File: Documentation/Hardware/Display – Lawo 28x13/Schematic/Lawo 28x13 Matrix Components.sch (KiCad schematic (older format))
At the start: 7 parts, among them IC1 FP2800A, P1 CONN_02X17, P2 CONN_01X03

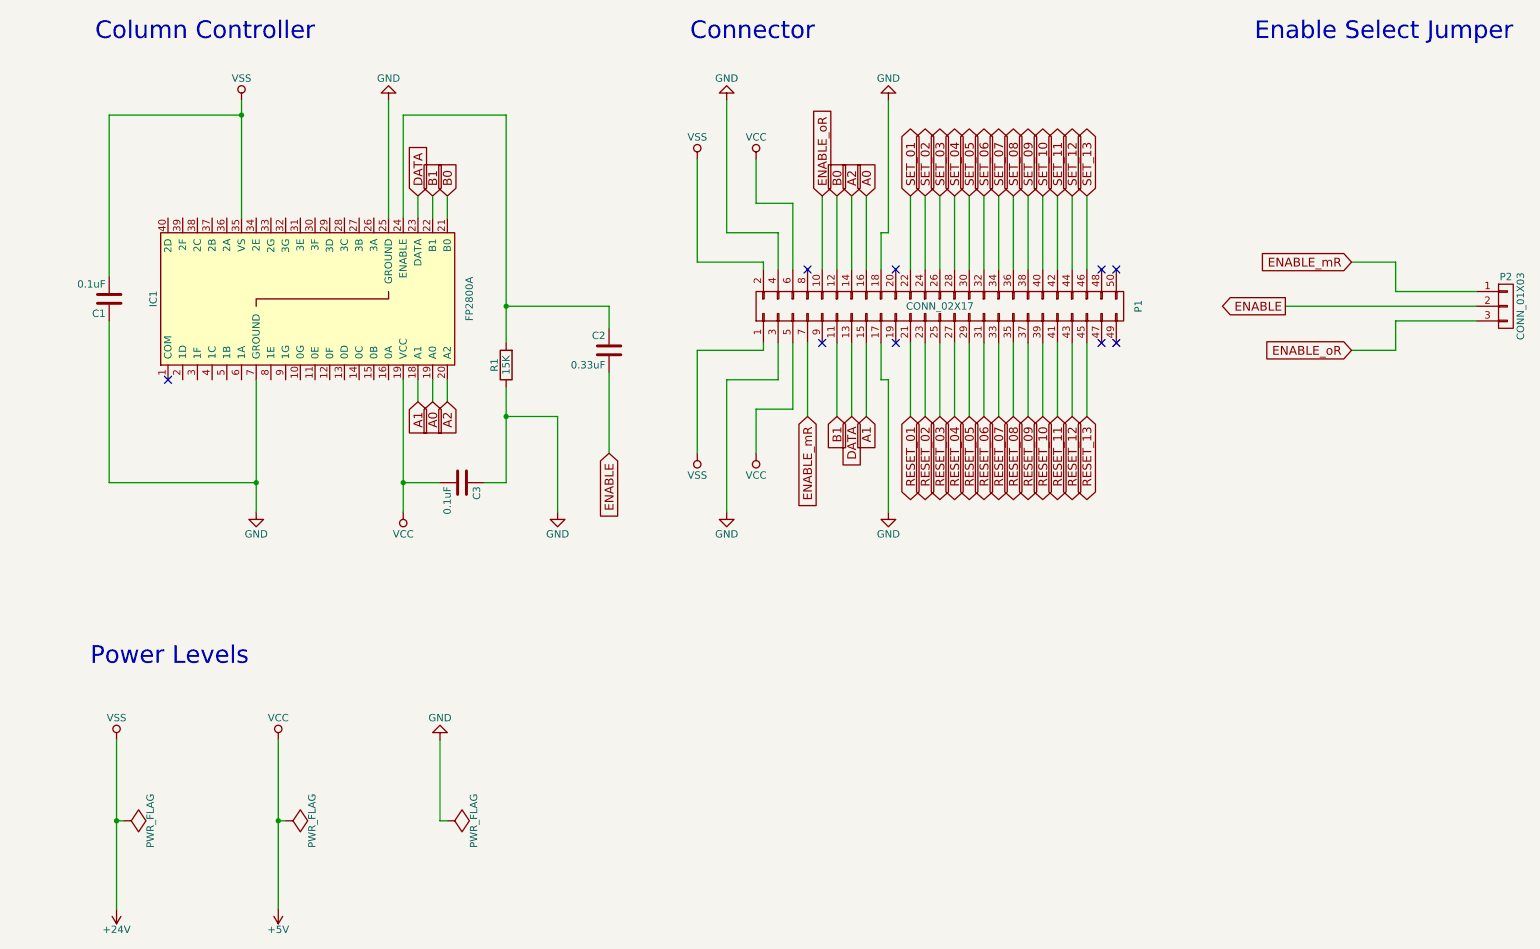
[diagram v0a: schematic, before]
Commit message: Hardware Lawo 28x13 Matrix Components schematic modified to orientate all components in the same direction plus fix to correct swapped pins.
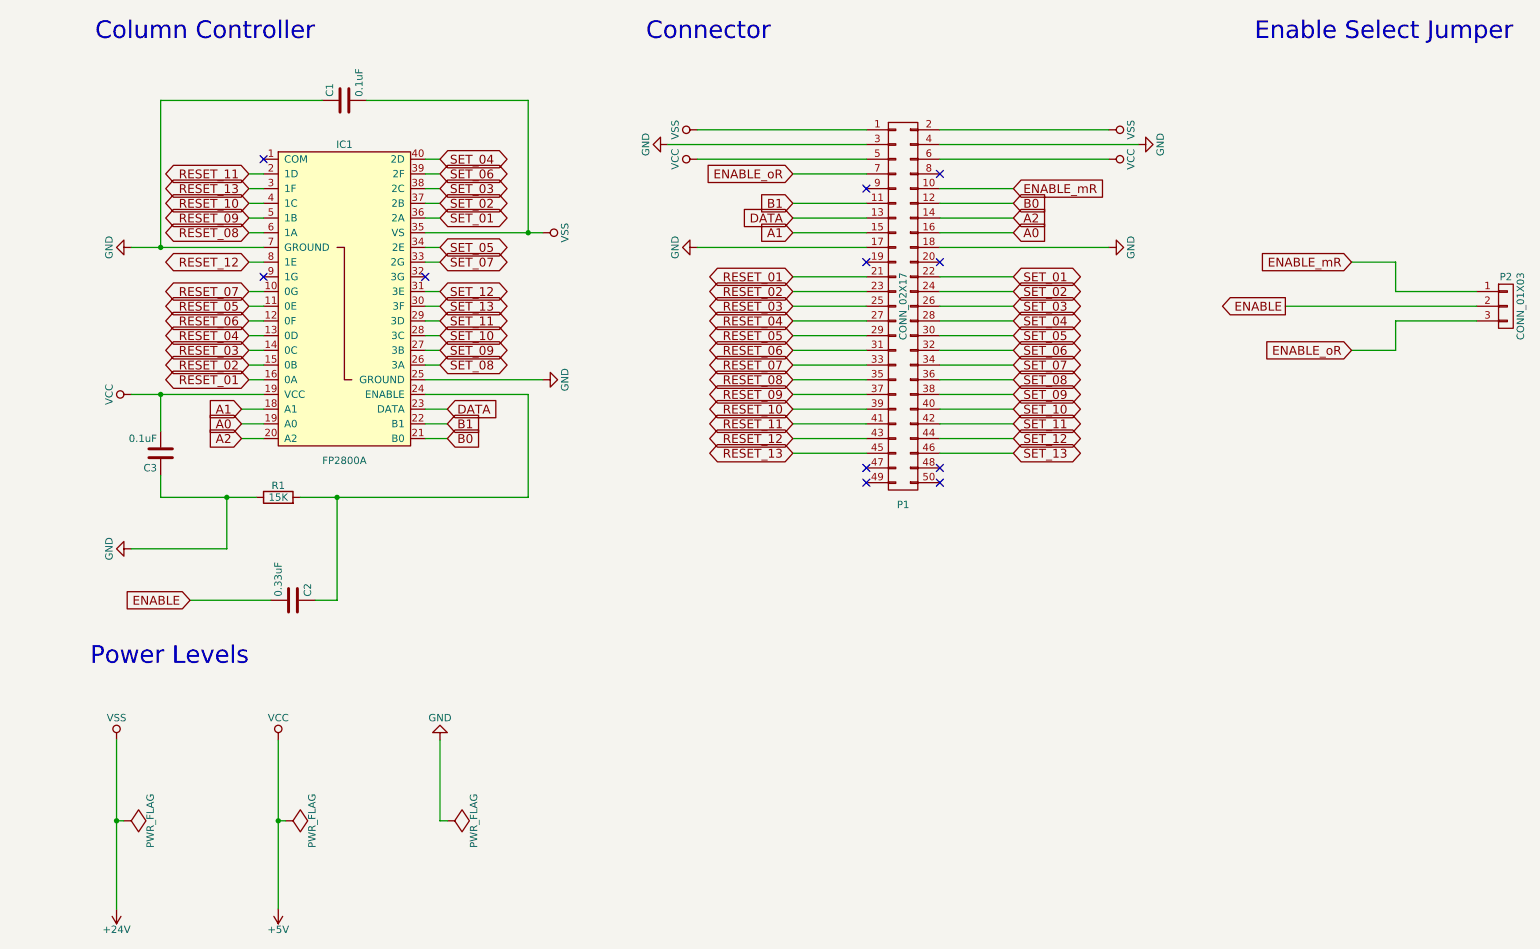
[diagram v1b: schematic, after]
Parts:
- P2: footprint (none) -> Pin_Headers:Pin_Header_Straight_1x03
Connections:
- net ENABLE_mR: now also P1.10 (P10); no longer P1.7 (P7)
- net ENABLE_oR: now also P1.7 (P7); no longer P1.10 (P10)
- net RESET_01: now also IC1.16 (0A)
- net RESET_02: now also IC1.15 (0B)
- net RESET_03: now also IC1.14 (0C)
- net RESET_04: now also IC1.13 (0D)
- net RESET_05: now also IC1.11 (0E)
- net RESET_06: now also IC1.12 (0F)
- net RESET_07: now also IC1.10 (0G)
- net RESET_08: now also IC1.6 (1A)
- net RESET_09: now also IC1.5 (1B)
- net RESET_10: now also IC1.4 (1C)
- net RESET_11: now also IC1.2 (1D)
- net RESET_12: now also IC1.8 (1E)
- net RESET_13: now also IC1.3 (1F)
- net SET_01: now also IC1.36 (2A)
- net SET_02: now also IC1.37 (2B)
- net SET_03: now also IC1.38 (2C)
- net SET_04: now also IC1.40 (2D)
- net SET_05: now also IC1.34 (2E)
- net SET_06: now also IC1.39 (2F)
- net SET_07: now also IC1.33 (2G)
- net SET_08: now also IC1.26 (3A)
- net SET_09: now also IC1.27 (3B)
- net SET_10: now also IC1.28 (3C)
- net SET_11: now also IC1.29 (3D)
- net SET_12: now also IC1.31 (3E)
- net SET_13: now also IC1.30 (3F)
- no-connect marks 9 -> 11
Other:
- moved on the sheet: C1, C2, C3, IC1, P1, R1
